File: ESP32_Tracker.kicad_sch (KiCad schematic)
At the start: 4 parts

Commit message: Layout completed
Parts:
- removed H4: MountingHole_Pad, MountingHole:MountingHole_2.2mm_M2_Pad_Via, symbol Mechanical:MountingHole_Pad
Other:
- moved on the sheet: H1, H2, H3

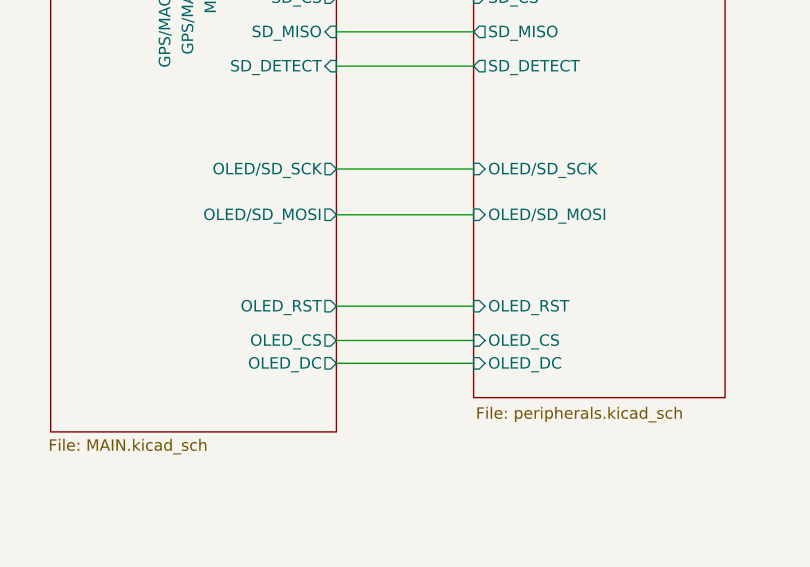
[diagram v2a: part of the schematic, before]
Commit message: changed to 8 pin connector
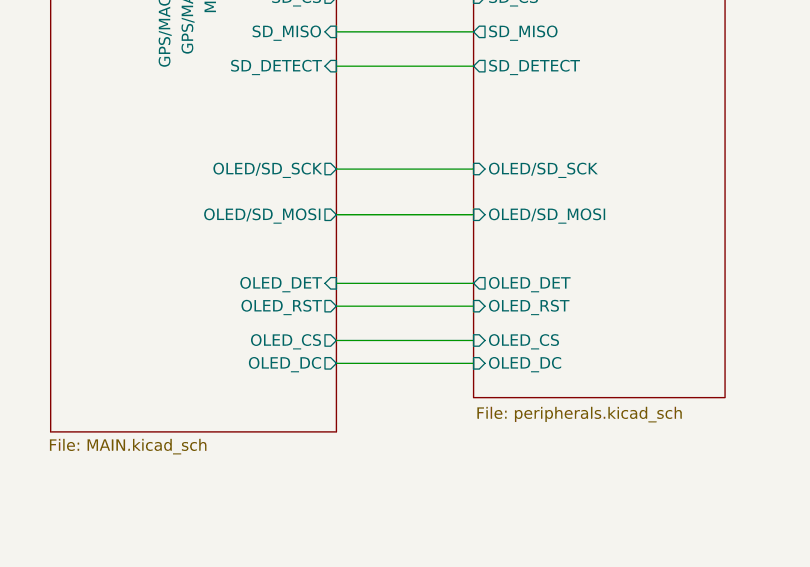
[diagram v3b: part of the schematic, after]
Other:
- sheet MCU/PWR ports: added OLED_DET; removed none
- sheet Peripherals ports: added OLED_DET; removed none
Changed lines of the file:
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@@
+	(wire
+		(pts
+			(xy 184.15 114.3) (xy 199.39 114.3)
+		)
+		(stroke
+			(width 0)
+			(type default)
+		)
+	)
 	(wire
 		(pts
@@
 			)
 		)
+		(pin "OLED_DET" output
+			(at 199.39 114.3 180)
+			(effects
+				(font
+					(size 1.27 1.27)
+				)
+				(justify left)
+			)
+		)
 		(instances
 			(project "ESP32_Tracker"
@@
 			(effects
 				(font
+					(size 1.27 1.27)
+				)
+				(justify right)
+			)
+		)
+		(pin "OLED_DET" input
+			(at 184.15 114.3 0)
+			(effects
+				(font
